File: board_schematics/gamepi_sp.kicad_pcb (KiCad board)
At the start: 2 copper layers, 29 parts, among them SW1 LED, SW10 R, SW11 L, SW12 Power Switch, SW2 UP, SW3 DOWN, SW4 LEFT, SW5 RIGHT, SW6 A, SW7 B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

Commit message: pcb design is hard :c
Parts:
- D1, R1, R10, R11, R12, R13, R14, R2, R3, R4, R5, R6, R7, R8, R9: footprint Resistor_SMD:R_0201_0603Metric -> Resistor_THT:R_Axial_DIN0204_L3.6mm_D1.6mm_P5.08mm_Horizontal
- moved R13 181.9 mm to (106.5, 123.0)
- moved R9 181.3 mm to (106.4, 130.5)
- moved R14 180.3 mm to (106.5, 120.5)
- moved R10 179.6 mm to (106.4, 128.0)
- moved R11 178.0 mm to (106.4, 125.5)
- moved SW11 172.8 mm to (95.0, 115.0)
- moved R8 170.6 mm to (119.0, 130.5), turned to 180 degrees
- moved R7 170.2 mm to (119.0, 128.0), turned to 180 degrees
- moved R6 170.0 mm to (119.0, 125.5), turned to 180 degrees
- moved R12 169.1 mm to (119.0, 118.0), turned to 180 degrees
- moved SW3 164.7 mm to (83.5, 83.5)
- moved R5 163.1 mm to (119.0, 123.0), turned to 180 degrees
- moved R4 162.8 mm to (119.0, 120.5), turned to 180 degrees
- moved SW9 153.0 mm to (128.2, 153.2)
- moved SW5 152.9 mm to (105.0, 106.0)
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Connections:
- R10 pad 1: Net-(U1-GPIO_1) -> Net-(U1-GPIO_16)
- R11 pad 1: Net-(U1-GPIO_7) -> Net-(U1-GPIO_20)
- R13 pad 1: Net-(U1-GPIO_20) -> Net-(U1-GPIO_21)
- R14 pad 1: Net-(U1-GPIO_21) -> Net-(U1-GPIO_26)
- R4 pad 1: Net-(U1-GPIO_26) -> Net-(U1-GPIO_24)
- R5 pad 1: Net-(U1-GPIO_8) -> Net-(U1-GPIO_25)
- R6 pad 1: Net-(U1-GPIO_25) -> Net-(U1-GPIO_8)
- R7 pad 1: Net-(U1-GPIO_24) -> Net-(U1-GPIO_7)
- R8 pad 1: Net-(U1-GPIO_16) -> Net-(U1-GPIO_1)
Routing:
- net Net-(SW1-Pad2): track 0.00 -> 223.2 mm
- net Net-(U1-GPIO_16): track 0.00 -> 49.6 mm
- net Net-(U1-GPIO_26): track 0.00 -> 41.7 mm
- net Net-(U1-GPIO_18): track 0.00 -> 30.0 mm
- net Net-(R10-Pad2): track 0.00 -> 29.7 mm
- net Net-(U1-GPIO_21): track 0.00 -> 21.3 mm
- net Net-(U1-GPIO_23): track 0.00 -> 21.1 mm
- net Net-(U1-GPIO_25): track 0.00 -> 20.1 mm
- net Net-(D1-K): track 0.00 -> 18.1 mm
- net Net-(U1-GPIO_8): track 0.00 -> 17.7 mm
- net Net-(U1-GPIO_24): track 0.00 -> 17.5 mm
- net Net-(SW12A-B): track 0.00 -> 15.4 mm
- net Net-(U1-GPIO_20): track 0.00 -> 12.2 mm
- net Net-(D1-A): track 0.00 -> 12.1 mm
- net Net-(U1-GPIO_12): track 0.00 -> 11.8 mm
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
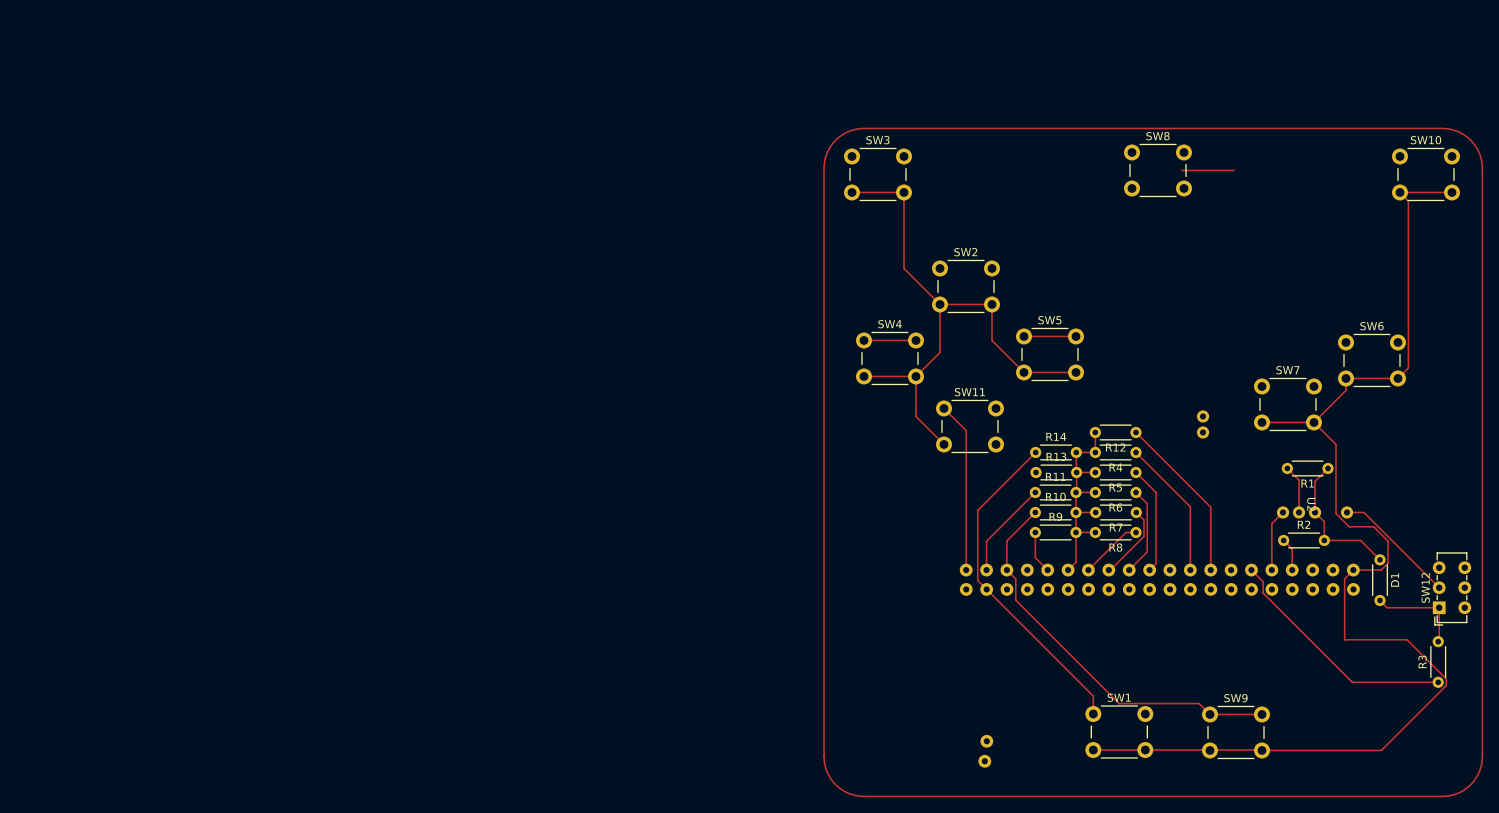
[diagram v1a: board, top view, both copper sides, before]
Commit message: restarting pcb layout with new approach
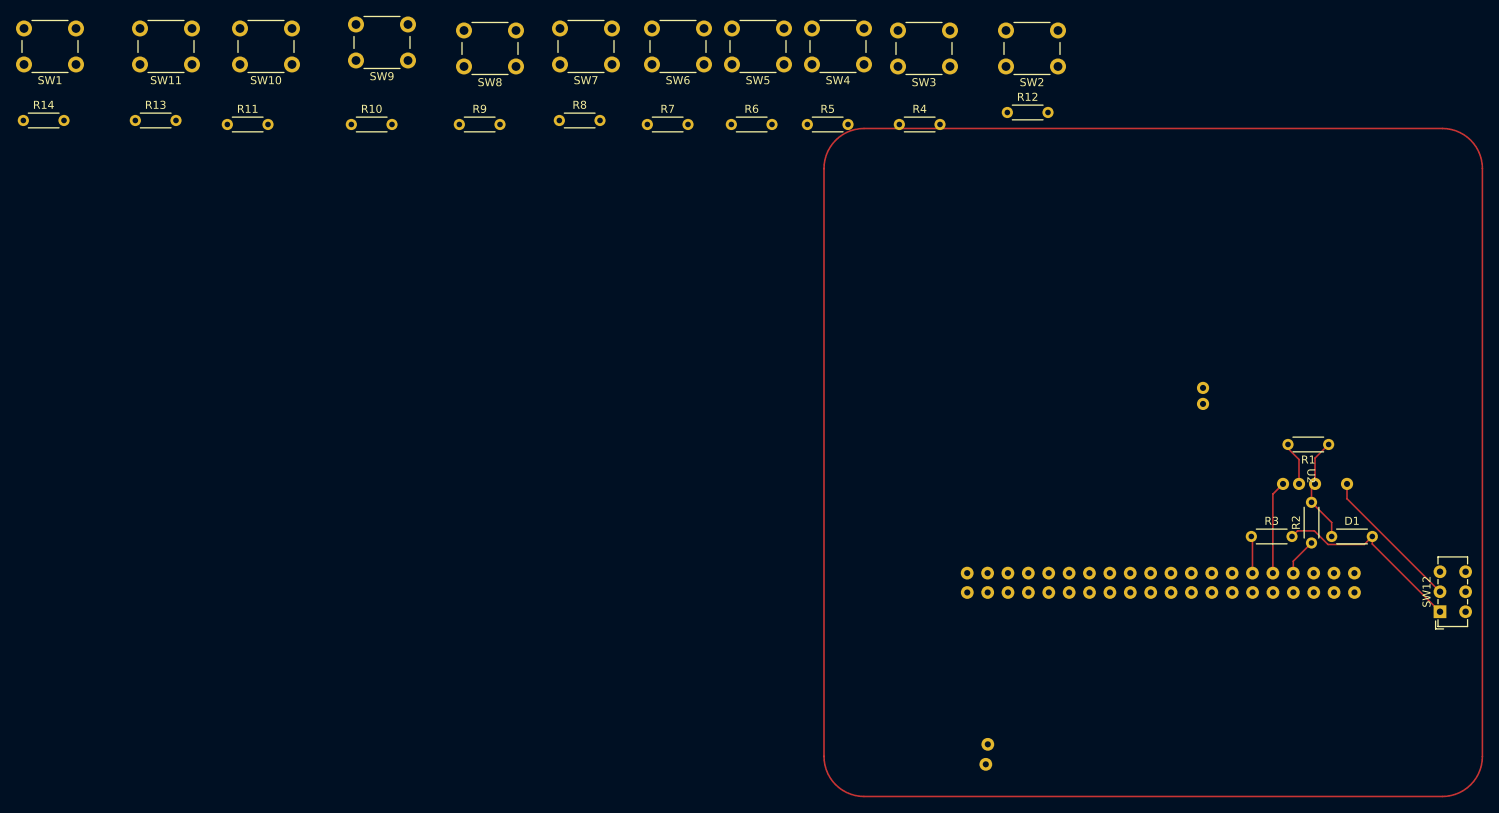
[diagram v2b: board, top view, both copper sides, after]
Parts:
- moved SW1 150.9 mm to (-13.5, 72.0), turned to 180 degrees
- moved SW10 139.0 mm to (13.5, 72.0), turned to 180 degrees
- moved R14 133.2 mm to (-20.1, 79.0)
- moved SW9 129.4 mm to (28.0, 71.5), turned to 180 degrees
- moved R13 120.9 mm to (-6.08, 79.0)
- moved R11 111.0 mm to (5.42, 79.5)
- moved SW11 103.4 mm to (1.00, 72.0), turned to 180 degrees
- moved R10 98.3 mm to (20.9, 79.5)
- moved SW7 90.7 mm to (53.5, 72.0), turned to 180 degrees
- moved R8 88.6 mm to (46.9, 79.0), turned to 0 degrees
- moved R9 88.2 mm to (34.4, 79.5)
- moved SW6 87.5 mm to (65.0, 72.0), turned to 180 degrees
- moved R7 78.0 mm to (57.9, 79.5), turned to 0 degrees
- moved SW8 77.7 mm to (41.5, 72.2), turned to 180 degrees
- moved R6 68.4 mm to (68.4, 79.5), turned to 0 degrees
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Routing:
- net Net-(SW1-Pad2): track 223.2 -> 0.00 mm
- net Net-(U1-GPIO_16): track 49.6 -> 0.00 mm
- net Net-(U1-GPIO_26): track 41.7 -> 0.00 mm
- net Net-(R10-Pad2): track 29.7 -> 0.00 mm
- net Net-(U1-GPIO_18): track 30.0 -> 4.64 mm
- net Net-(U1-GPIO_21): track 21.3 -> 0.00 mm
- net Net-(U1-GPIO_23): track 21.1 -> 0.00 mm
- net Net-(U1-GPIO_25): track 20.1 -> 0.00 mm
- net Net-(U1-GPIO_8): track 17.7 -> 0.00 mm
- net Net-(U1-GPIO_24): track 17.5 -> 0.00 mm
- net Net-(D1-A): track 12.1 -> 24.4 mm
- net Net-(U1-GPIO_20): track 12.2 -> 0.00 mm
- net Net-(U1-GPIO_12): track 11.8 -> 0.00 mm
- net Net-(U1-GPIO_7): track 9.53 -> 0.00 mm
- net Net-(U1-GPIO_1): track 7.89 -> 0.00 mm
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
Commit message: another pcb attempt, this time more succesful
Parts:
- moved R14 163.8 mm to (127.3, 150.5)
- moved SW1 163.0 mm to (127.2, 154.2), turned to 0 degrees
- moved R13 139.4 mm to (113.5, 150.5)
- moved SW11 139.2 mm to (113.5, 154.0), turned to 0 degrees
- moved R10 89.5 mm to (96.4, 127.5)
- moved SW9 86.3 mm to (96.5, 124.0)
- moved SW10 85.8 mm to (88.0, 114.5)
- moved R11 85.2 mm to (81.5, 117.9), turned to -90 degrees
- moved R9 81.3 mm to (105.5, 118.9), turned to -90 degrees
- moved SW8 77.2 mm to (105.5, 115.5)
- moved SW4 75.6 mm to (159.0, 87.5)
- moved R5 75.4 mm to (152.5, 90.4), turned to -90 degrees
- moved R8 59.3 mm to (99.9, 105.5)
- moved SW3 58.1 mm to (141.5, 108.0)
- moved SW2 57.4 mm to (156.0, 105.5)
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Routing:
- net Net-(R10-Pad2): track 0.00 -> 345.3 mm
- net Net-(SW1-Pad2): track 0.00 -> 279.5 mm
- net Net-(U1-GPIO_25): track 0.00 -> 64.9 mm
- net Net-(U1-GPIO_7): track 0.00 -> 60.4 mm
- net Net-(U1-GPIO_8): track 0.00 -> 47.9 mm
- net Net-(U1-GPIO_1): track 0.00 -> 43.6 mm
- net Net-(U1-GPIO_23): track 0.00 -> 40.2 mm
- net Net-(U1-GPIO_20): track 0.00 -> 36.2 mm
- net Net-(U1-GPIO_26): track 0.00 -> 35.8 mm
- net Net-(U1-GPIO_24): track 0.00 -> 31.3 mm
- net Net-(U1-GPIO_12): track 0.00 -> 27.7 mm
- net Net-(U1-GPIO_21): track 0.00 -> 26.2 mm
- net Net-(U1-GPIO_16): track 0.00 -> 20.8 mm

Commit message: pcb design that i am happy with
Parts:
- moved SW4 38.6 mm to (130.2, 113.2), turned to 0 degrees
- moved R5 29.6 mm to (130.2, 109.8), turned to 0 degrees
- moved SW10 27.0 mm to (89.5, 87.5)
- moved R11 27.0 mm to (83.0, 91.0)
- moved R7 22.7 mm to (105.5, 107.5)
- moved SW7 20.9 mm to (112.0, 119.5)
- moved SW6 20.6 mm to (96.0, 107.5), turned to 0 degrees
- moved R12 20.4 mm to (159.0, 91.0), turned to 180 degrees
- moved R8 18.3 mm to (105.4, 123.0)
- moved SW2 18.2 mm to (159.0, 87.5)
- moved R9 15.0 mm to (95.9, 130.5), turned to 0 degrees
- moved SW8 11.9 mm to (102.5, 127.0)
- moved R6 11.1 mm to (118.5, 103.0)
- moved R10 11.0 mm to (86.5, 122.8)
- moved SW5 10.7 mm to (125.0, 99.2)
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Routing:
- net Net-(R10-Pad2): track 345.3 -> 243.1 mm
- net Net-(U2-Supply_GND): track 0.00 -> 89.6 mm
- net Net-(U2-Supply_5V): track 0.00 -> 73.4 mm
- net Net-(SW1-Pad2): track 279.5 -> 339.6 mm
- net Net-(U1-GPIO_23): track 40.2 -> 73.3 mm
- net Net-(U1-GPIO_20): track 36.2 -> 63.8 mm
- net Net-(U1-GPIO_25): track 64.9 -> 39.7 mm
- net Net-(U1-GPIO_7): track 60.4 -> 42.2 mm
- net Net-(U1-GPIO_1): track 43.6 -> 25.6 mm
- net Net-(U1-GPIO_24): track 31.3 -> 46.6 mm
- net Net-(U1-GPIO_16): track 20.8 -> 31.2 mm
- net Net-(U1-GPIO_26): track 35.8 -> 28.0 mm
- net Net-(U1-GPIO_12): track 27.7 -> 20.7 mm
- net Net-(D1-K): track 13.4 -> 7.15 mm
- net Net-(U1-GPIO_21): track 26.2 -> 19.9 mm
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
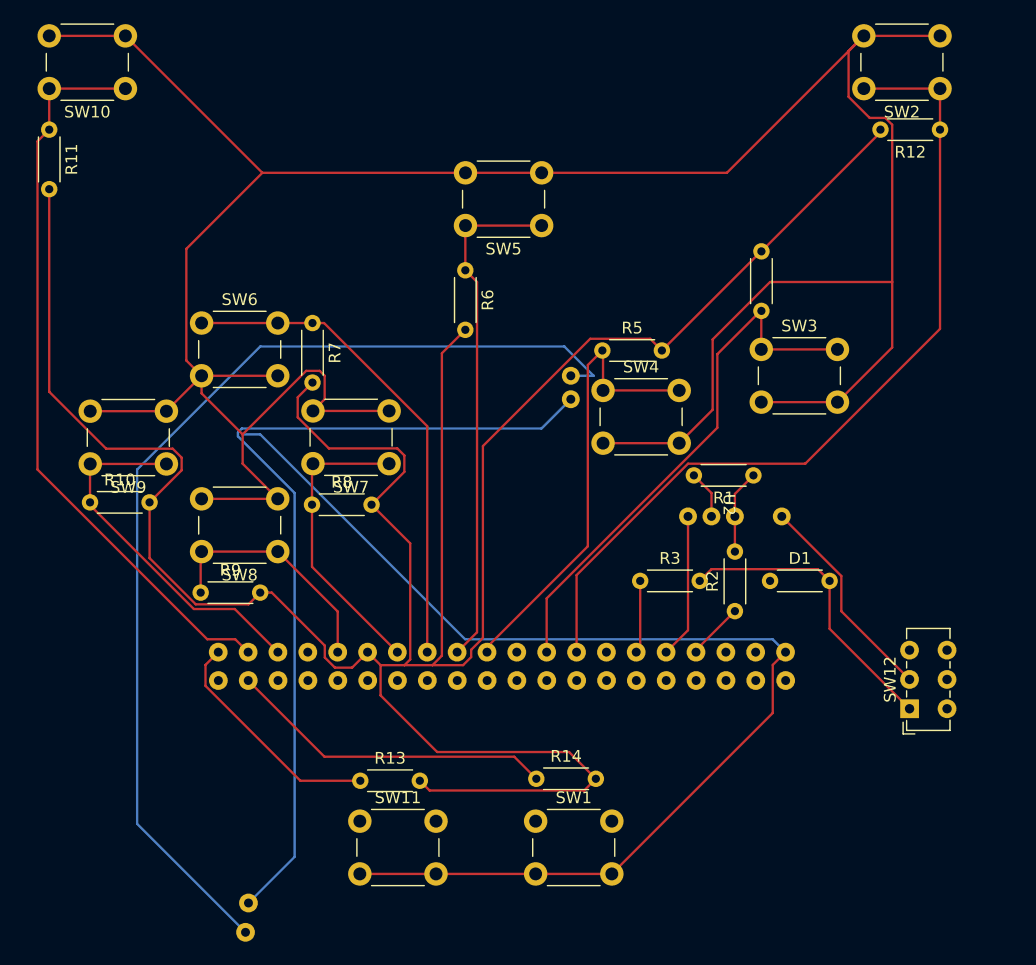
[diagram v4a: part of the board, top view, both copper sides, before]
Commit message: added future opportunities to docs
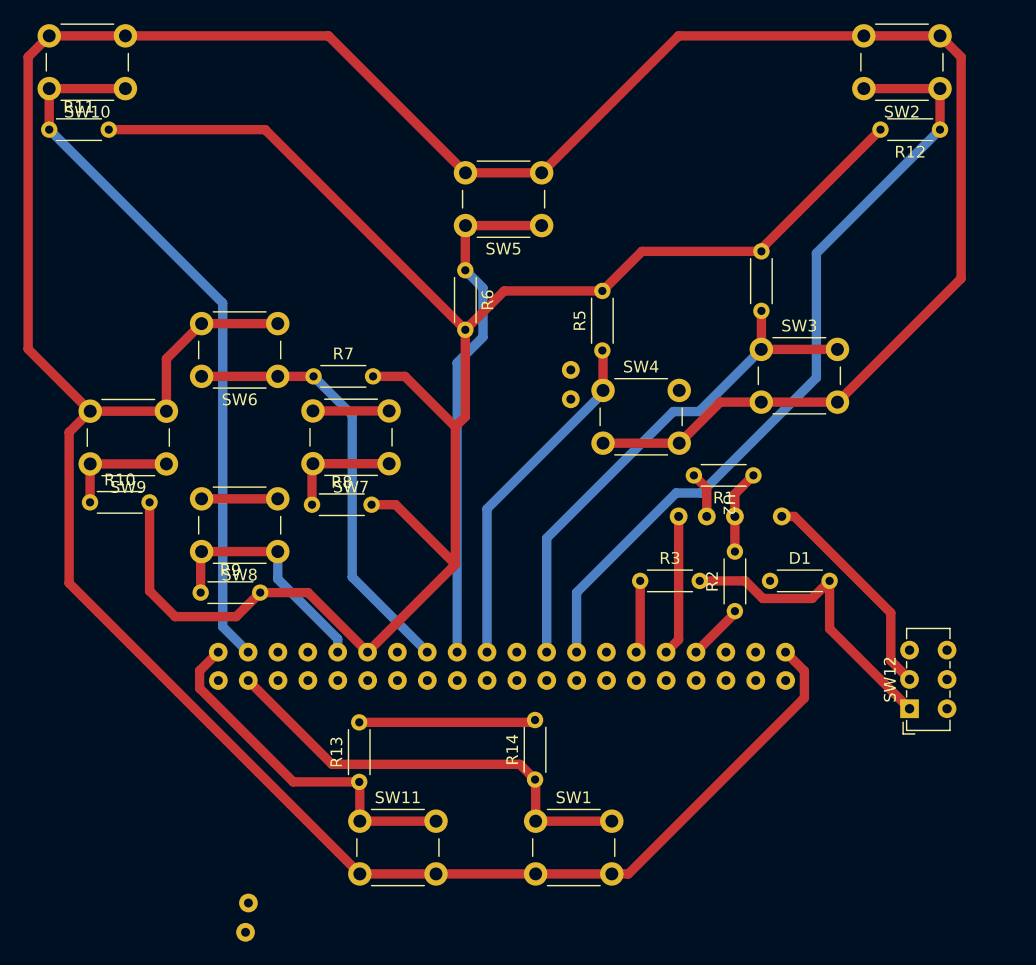
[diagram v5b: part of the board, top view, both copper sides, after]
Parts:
- moved SW6 7.93 mm to (102.5, 112.0), turned to 180 degrees
- moved R7 4.55 mm to (105.5, 112.0), turned to 0 degrees
- moved R13 0.13 mm to (109.5, 146.7), turned to 90 degrees
- moved R14 0.13 mm to (124.5, 146.4), turned to 90 degrees
- turned R11 to 0 degrees
- turned R5 to 90 degrees
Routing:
- net Net-(U2-Supply_GND): track 89.6 -> 0.00 mm
- net Net-(U2-Supply_5V): track 73.4 -> 0.02 mm
- net Net-(R10-Pad2): track 243.1 -> 174.2 mm
- net Net-(SW1-Pad2): track 339.6 -> 312.4 mm
- net Net-(U1-GPIO_16): track 31.2 -> 9.78 mm
- net Net-(U1-GPIO_1): track 25.6 -> 10.0 mm
- net Net-(U1-GPIO_21): track 19.9 -> 30.5 mm
- net Net-(U1-GPIO_26): track 28.0 -> 38.0 mm
- net Net-(U1-GPIO_25): track 39.7 -> 29.9 mm
- net Net-(U1-GPIO_7): track 42.2 -> 37.1 mm
- net Net-(U1-GPIO_23): track 73.3 -> 68.7 mm
- net Net-(U1-GPIO_20): track 63.8 -> 61.6 mm
- net Net-(U1-GPIO_24): track 46.6 -> 44.5 mm
- net Net-(SW12A-B): track 18.4 -> 19.1 mm
